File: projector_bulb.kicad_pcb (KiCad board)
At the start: 2 copper layers, 85.4 x 85.3 mm, 28 parts, among them J1 AC_1, J10 mount_2, J3 AC_2, J9 mount_1, U1 AL8860, U2 L7815

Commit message: Revision 2, still needs documentation and things
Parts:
- removed JP2: Jumper_2_Bridged, Jumper:SolderJumper-2_P1.3mm_Bridged_RoundedPad1.0x1.5mm
- added JP1: Jumper_2_Bridged, Jumper:SolderJumper-2_P1.3mm_Bridged_RoundedPad1.0x1.5mm, F.Cu at (140.7, 15.4)
- C1, C2: footprint Capacitor_THT:CP_Radial_D16.0mm_P7.50mm -> Capacitor_THT:CP_Radial_D12.5mm_P5.00mm
- C5: value 4.7u -> 22u
- R2: value 51k -> 7.5k
- U1: value AL8860 -> PAM2863; footprint Package_TO_SOT_SMD:TSOT-23-5_HandSoldering -> Package_SO:HTSOP-8-1EP_3.9x4.9mm_P1.27mm_EP2.4x3.2mm
- U2: value L7815 -> AP7381-33Y; footprint Package_TO_SOT_SMD:TO-263-2 -> Package_TO_SOT_SMD:SOT-89-3
- moved C5 11.0 mm to (117.3, 57.7), turned to 90 degrees
- moved D2 9.27 mm to (111.8, 45.7), turned to 90 degrees
- moved U1 6.40 mm to (112.8, 57.6), turned to 270 degrees
- moved R1 4.81 mm to (118.4, 50.3), turned to 180 degrees
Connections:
- C5 pad 1: Net-(C5-Pad1) -> GND_UPRIGHT
- C5 pad 2: Net-(C5-Pad2) -> VIN_UPRIGHT
- D2 pad 1: Net-(C5-Pad1) -> VIN_UPRIGHT
- J10 pad 1: Net-(J10-Pad1) -> (no net)
- J9 pad 1: Net-(J9-Pad1) -> (no net)
- R1 pad 1: Net-(C5-Pad1) -> VIN_UPRIGHT
- R2 pad 1: Net-(C5-Pad1) -> Net-(R2-Pad1)
- REF** pad 1: Net-(C5-Pad2) -> GND_UPRIGHT (x2)
- REF** pad 1: Net-(J5-Pad1) -> VIN_UPRIGHT (x2)
- RV1 pad 1: Net-(C5-Pad2) -> Net-(R2-Pad1)
- RV1 pad 3: Net-(R2-Pad2) -> GND_UPRIGHT
- U1 pad 1: Net-(D2-Pad2) -> VIN_UPRIGHT
- U1 pad 2: Net-(C5-Pad2) -> Net-(J8-Pad1)
- U1 pad 3: Net-(JP2-Pad1) -> GND_UPRIGHT
- U1 pad 4: Net-(J8-Pad1) -> DIMMING
- U1 pad 5: Net-(C5-Pad1) -> Net-(D2-Pad2)
- U2 pad 1: Net-(J5-Pad1) -> Net-(R2-Pad2)
- U2 pad 2: Net-(C5-Pad2) -> GND_UPRIGHT
- U2 pad 3: Net-(C5-Pad1) -> VIN_UPRIGHT
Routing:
- net GND_UPRIGHT: track 0.00 -> 125.3 mm, vias 0 -> 2
- net Net-(C5-Pad2): track 111.7 -> 0.00 mm, vias 11 -> 0
- net Net-(C5-Pad1): track 104.8 -> 0.00 mm, vias 2 -> 0
- net VIN_UPRIGHT: track 0.00 -> 77.7 mm, vias 0 -> 1
- net DIMMING: track 0.00 -> 67.0 mm, vias 0 -> 2
- net Net-(R2-Pad2): track 6.84 -> 67.8 mm, vias 0 -> 2
- net Net-(JP1-Pad1): track 53.4 -> 5.39 mm
- net Net-(J5-Pad1): track 22.0 -> 0.00 mm, vias 1 -> 0
- net Net-(JP2-Pad1): track 17.9 -> 0.00 mm, vias 1 -> 0
- net Net-(J8-Pad1): track 53.1 -> 44.0 mm, vias 2 -> 8
- net Net-(R2-Pad1): track 0.00 -> 9.05 mm
- net Net-(J7-Pad1): track 29.1 -> 22.5 mm, vias 1 -> 7
- net Net-(D2-Pad2): track 49.4 -> 50.6 mm
- removed copper zone on B.Cu, net Net-(C5-Pad2)
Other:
- board text added: "LED DCA Lamp Revision 2 April 2021"
- board text added: "LED front on this side"
- board text added: "ettingersam@gmail.com"

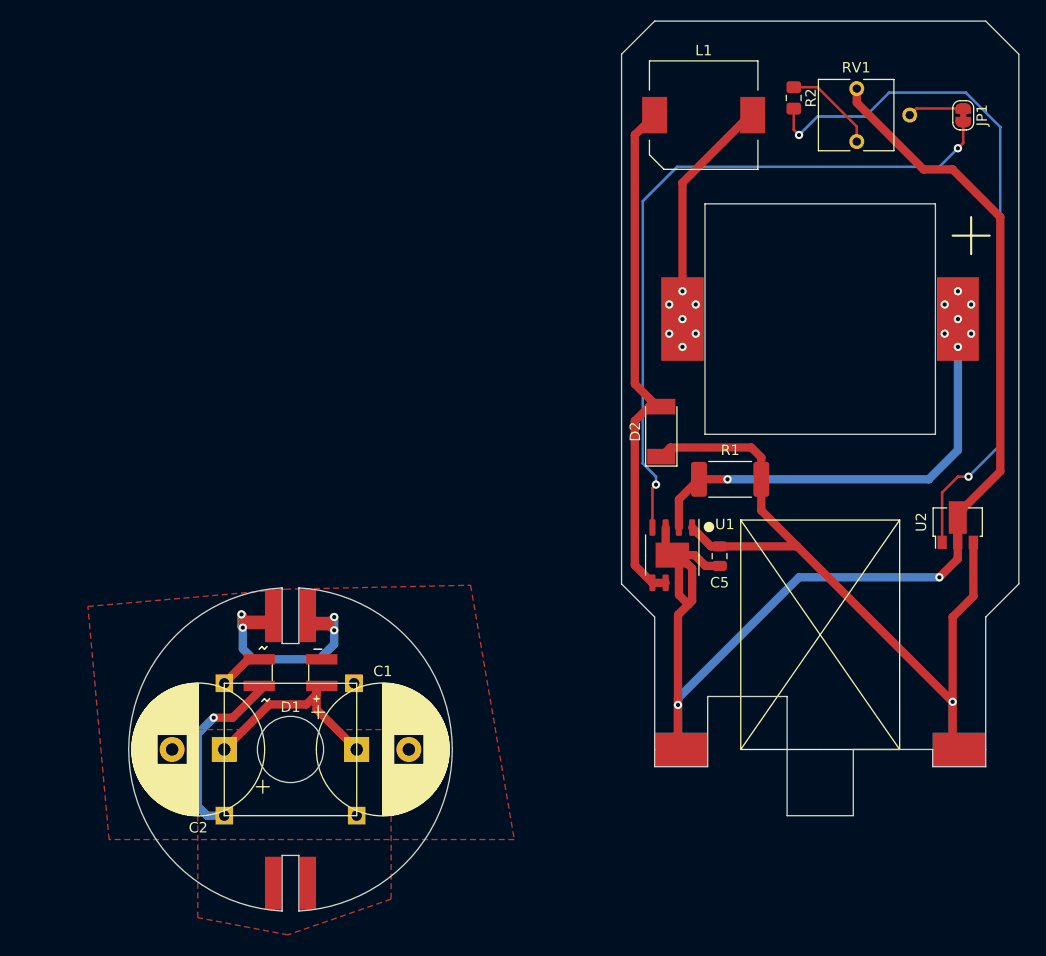
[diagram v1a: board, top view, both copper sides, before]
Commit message: Much progress on Aluminum PCB
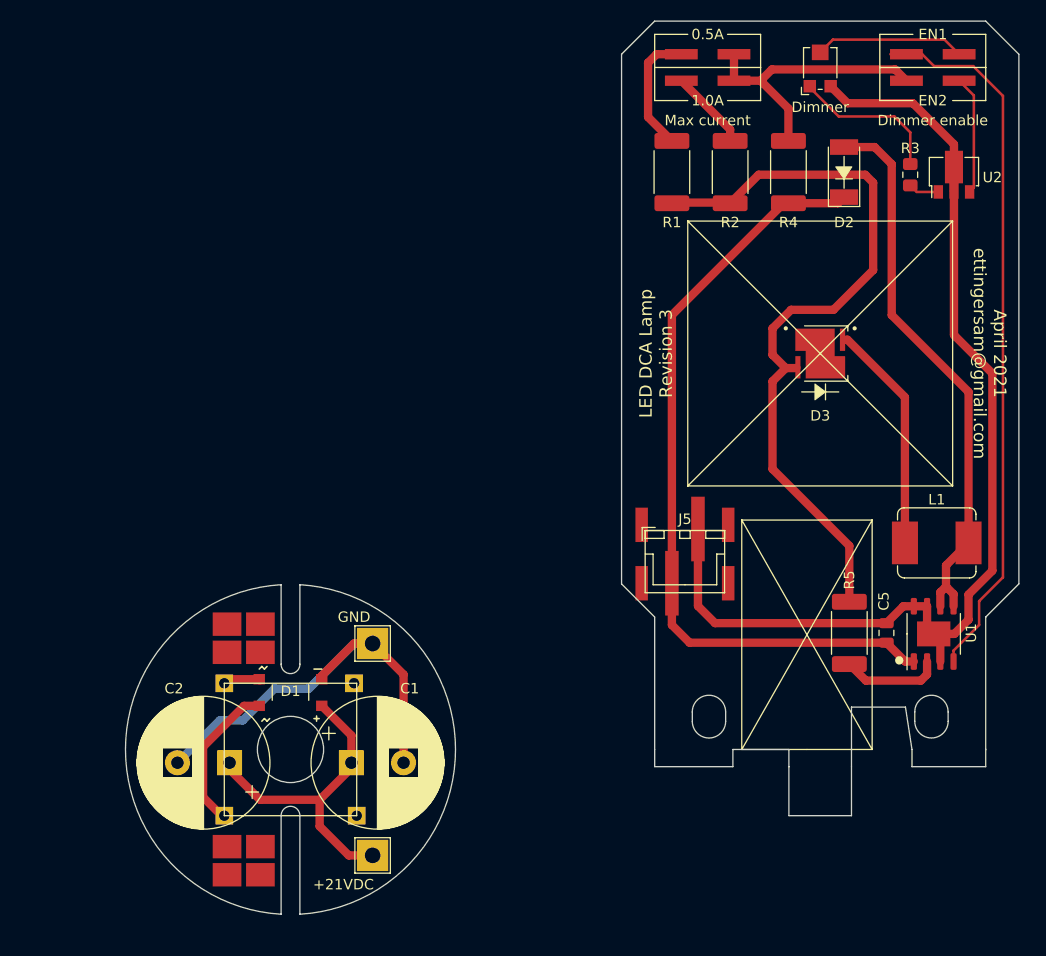
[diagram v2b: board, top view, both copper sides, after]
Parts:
- removed JP1: Jumper_2_Bridged, Jumper:SolderJumper-2_P1.3mm_Bridged_RoundedPad1.0x1.5mm
- removed REF** (x12): angle_joint, projector_bulb:angle_joint
- added +21VDC: to_upright_+, TestPoint:TestPoint_THTPad_3.0x3.0mm_Drill1.5mm, F.Cu at (84.1, 86.4)
- added D3: LED_Small_ALT, LED_SMD:LED_Cree-XHP50_12V, F.Cu at (127.0, 38.2)
- added GND: to_upright_-, TestPoint:TestPoint_THTPad_3.0x3.0mm_Drill1.5mm, F.Cu at (84.1, 66.0)
- added J11: mount_2, projector_bulb:wuerth_7466303R, F.Cu at (71.7, 65.5)
- added J12: mount_1, projector_bulb:wuerth_7466303R, F.Cu at (71.7, 86.9)
- added J5: to_base, projector_bulb:JST_XA_1x02_P2.50mm_SMD, F.Cu at (112.8, 57.7)
- added J7: Conn_02x02_Odd_Even, Connector_PinHeader_2.54mm:PinHeader_2x02_P2.54mm_Vertical_SMD, F.Cu at (116.2, 10.8)
- added J8: Conn_02x02_Odd_Even, Connector_PinHeader_2.54mm:PinHeader_2x02_P2.54mm_Vertical_SMD, F.Cu at (137.8, 10.8)
- added R2: 0.200, Resistor_SMD:R_2512_6332Metric_Pad1.52x3.35mm_HandSolder, F.Cu at (118.4, 20.8)
- added R4: 0Ω, Resistor_SMD:R_2512_6332Metric_Pad1.52x3.35mm_HandSolder, F.Cu at (124.0, 20.8)
- added R5: 0Ω, Resistor_SMD:R_2512_6332Metric_Pad1.52x3.35mm_HandSolder, F.Cu at (129.8, 65.0)
- C1, C2: value 2200u -> 1000μ
- L1: footprint projector_bulb:L_Wuerth_WE-PD-100100 -> projector_bulb:L_KEMET_MPLCV_0654_7.9x6.5mm
- RV1: footprint Potentiometer_THT:Potentiometer_Vishay_T73YP_Vertical -> Potentiometer_SMD:Potentiometer_Bourns_TC33X_Vertical
- moved L1 46.7 mm to (138.2, 56.4)
- moved U2 33.6 mm to (139.8, 21.1)
- moved D2 30.4 mm to (129.3, 20.8)
- moved R1 30.0 mm to (112.8, 20.8), turned to 270 degrees
- moved U1 26.2 mm to (137.9, 65.1), turned to 90 degrees
- moved C5 17.6 mm to (133.3, 65.0), turned to 270 degrees
- moved R3 13.4 mm to (135.6, 21.1)
- moved RV1 7.92 mm to (127.0, 10.8), turned to 90 degrees
- moved D1 1.91 mm to (76.2, 70.7)
- moved C2 1.37 mm to (70.4, 77.5)
- moved C1 1.37 mm to (82.0, 77.5)
- renumbered R2 to R3
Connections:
- net GND renamed GND_BASE
- net Net-(C1-Pad1) renamed VIN_BASE
- L1 pad 1: Net-(D2-Pad2) -> Net-(D3-Pad1)
- L1 pad 2: Net-(J7-Pad1) -> Net-(D2-Pad2)
- R1 pad 1: VIN_UPRIGHT -> Net-(J7-Pad1)
- R1 pad 2: Net-(J8-Pad1) -> CURRENT_SELECT
- U1 pad 2: Net-(J8-Pad1) -> Net-(R5-Pad2)
- U2 pad 3: VIN_UPRIGHT -> Net-(J8-Pad4)
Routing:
- net CURRENT_SELECT: track 0.00 -> 72.6 mm
- net Net-(R3-Pad2): track 67.8 -> 2.95 mm, vias 2 -> 0
- net Net-(J8-Pad1): track 44.0 -> 0.00 mm, vias 8 -> 0
- net VIN_NET_TIE: track 0.00 -> 26.9 mm
- net GND_UPRIGHT: track 125.3 -> 102.6 mm, vias 2 -> 0
- net Net-(D3-Pad1): track 0.00 -> 22.1 mm
- net GND_BASE: track 30.3 -> 42.6 mm, vias 4 -> 0
- net Net-(J8-Pad4): track 0.00 -> 11.4 mm
- net Net-(J7-Pad1): track 22.5 -> 12.0 mm, vias 7 -> 0
- net VIN_BASE: track 19.5 -> 29.3 mm
- net Net-(R5-Pad2): track 0.00 -> 9.59 mm
- net Net-(J8-Pad2): track 5.39 -> 14.4 mm
- net Net-(J7-Pad3): track 0.00 -> 7.72 mm
- net Net-(R3-Pad1): track 9.05 -> 14.6 mm
- net Net-(D2-Pad2): track 50.6 -> 54.7 mm
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- removed copper zone on F.Cu, net GND_BASE
- removed copper zone on F.Cu, net VIN_BASE
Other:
- board size 85.4 x 85.3 mm -> 85.7 x 85.7 mm
- board text added: "0.5A"
- board text added: "1.0A"
- board text added: "April 2021 ettingersam@gmail.com"
- board text added: "Dimmer"
- board text added: "Dimmer enable"
- board text added: "EN1"
- board text added: "EN2"
- board text added: "LED DCA Lamp Revision 3"
- board text added: "Max current"
- board text removed: "LED DCA Lamp Revision 2 April 2021"
- board text removed: "LED front on this side"
- board text removed: "ettingersam@gmail.com"

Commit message: More changes, about to add some safety circuitry
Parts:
- added R6: 1M, Resistor_SMD:R_0805_2012Metric_Pad1.15x1.40mm_HandSolder, F.Cu at (85.9, 69.8)
- added REF**: Fuse_1206_3216Metric, Fuse:Fuse_1206_3216Metric, F.Cu at (69.2, 65.0)
- added REF**: LENS_LEDIL_CA16370_HB-SQ-W, projector_bulb:LENS_LEDIL_CA16370_HB-SQ-W, F.Cu at (127.0, 38.2)
- J11, J12: footprint projector_bulb:wuerth_7466303R -> projector_bulb:wuerth_7466310R
- J5: footprint projector_bulb:JST_XA_1x02_P2.50mm_SMD -> Connector_Molex:Molex_CLIK-Mate_505405-0270_1x02-1MP_P1.50mm_Vertical
- moved J12 1.97 mm to (73.4, 87.9), turned to 90 degrees
- moved J11 1.97 mm to (73.4, 64.5), turned to 90 degrees
- moved J5 1.08 mm to (113.5, 56.9)
- renumbered +21VDC to J2, GND to J4
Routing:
- net VIN_BASE: track 29.3 -> 35.5 mm
- net GND_UPRIGHT: track 102.6 -> 98.5 mm
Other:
- outline, holes or cut-outs redrawn

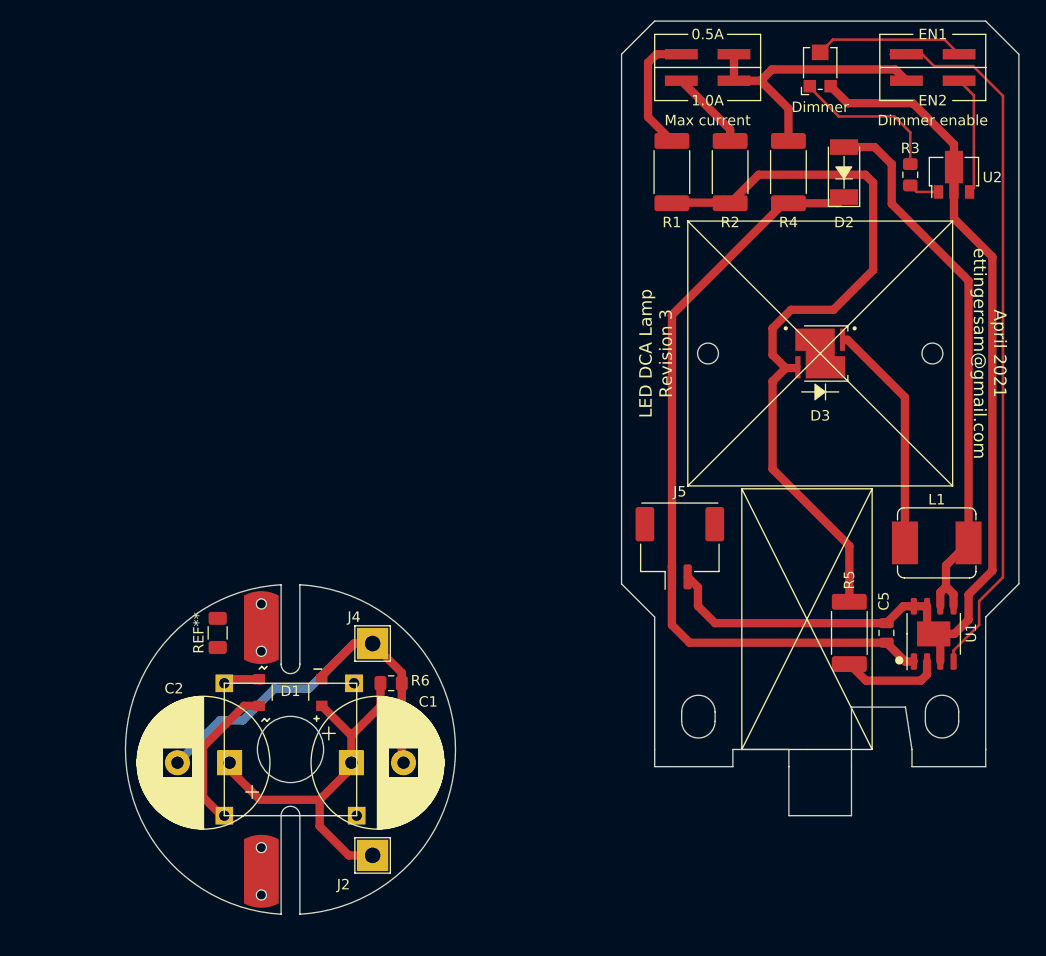
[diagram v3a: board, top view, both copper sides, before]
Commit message: Cleaned up schematic, working on documentation next
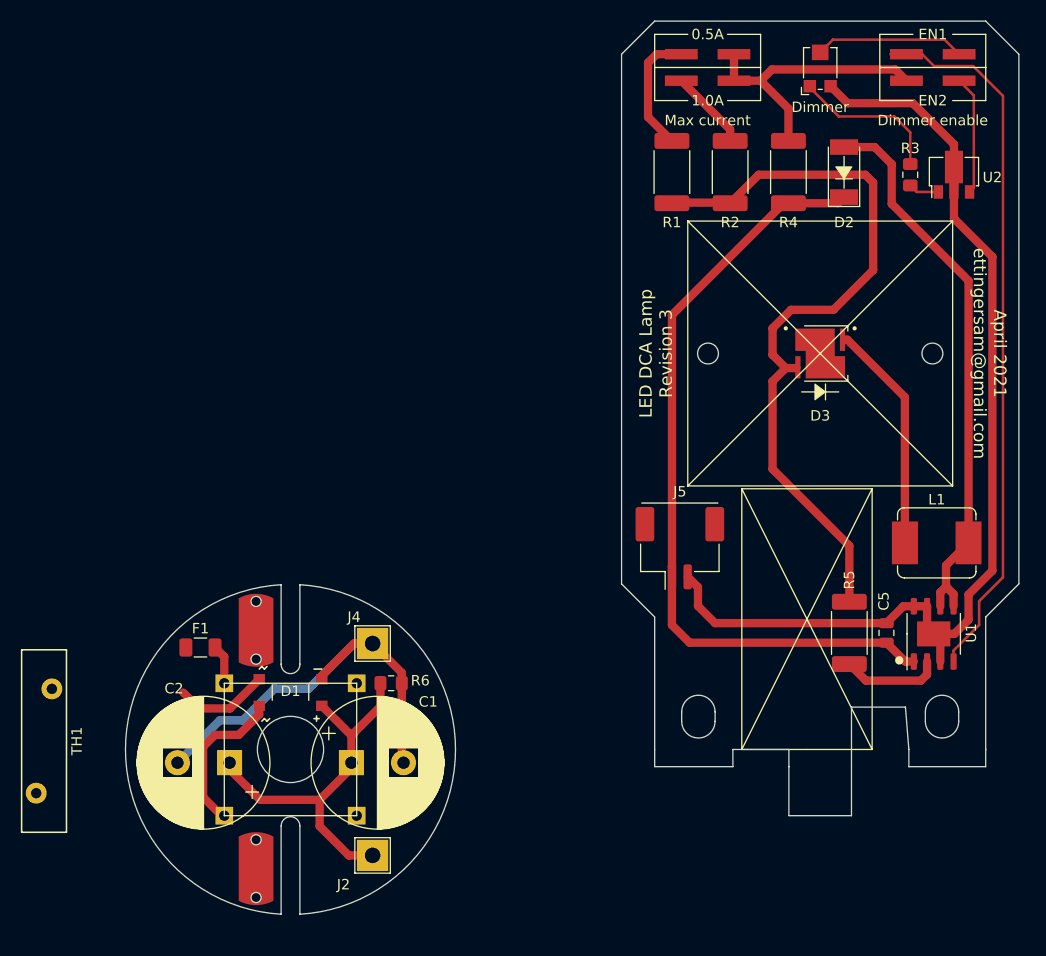
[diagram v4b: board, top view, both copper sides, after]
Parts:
- removed J1: AC_1, Connector_PinSocket_2.54mm:PinSocket_1x01_P2.54mm_Vertical
- removed J10: mount_2, Connector_PinSocket_2.54mm:PinSocket_1x01_P2.54mm_Vertical
- removed J11: mount_2, projector_bulb:wuerth_7466310R
- removed J12: mount_1, projector_bulb:wuerth_7466310R
- removed J3: AC_2, Connector_PinSocket_2.54mm:PinSocket_1x01_P2.54mm_Vertical
- removed J9: mount_1, Connector_PinSocket_2.54mm:PinSocket_1x01_P2.54mm_Vertical
- removed the REF** at (69.2, 65.0)
- added F1: Fuse, Fuse:Fuse_1206_3216Metric, F.Cu at (67.6, 66.4)
- added H1: MountingHole, projector_bulb:wuerth_7466310R, F.Cu at (72.9, 64.8)
- added H2: MountingHole, projector_bulb:wuerth_7466310R, F.Cu at (72.9, 87.6)
- added LA1: Lamp, projector_bulb:GX17q, B.Cu at (76.2, 76.2)
- added TH1: Thermistor_NTC, Varistor:RV_Disc_D21.5mm_W4.3mm_P10mm, F.Cu at (51.8, 80.4)
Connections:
- net CURRENT_SELECT renamed Net-(D3-Pad2)
- net VIN_NET_TIE renamed Net-(J7-Pad2)
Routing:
- net Net-(D1-Pad3): track 3.61 -> 9.25 mm
- net Net-(F1-Pad2): track 0.00 -> 3.80 mm
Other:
- outline, holes or cut-outs redrawn

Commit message: Add test points, replaced some expensive components with cheaper alternatives
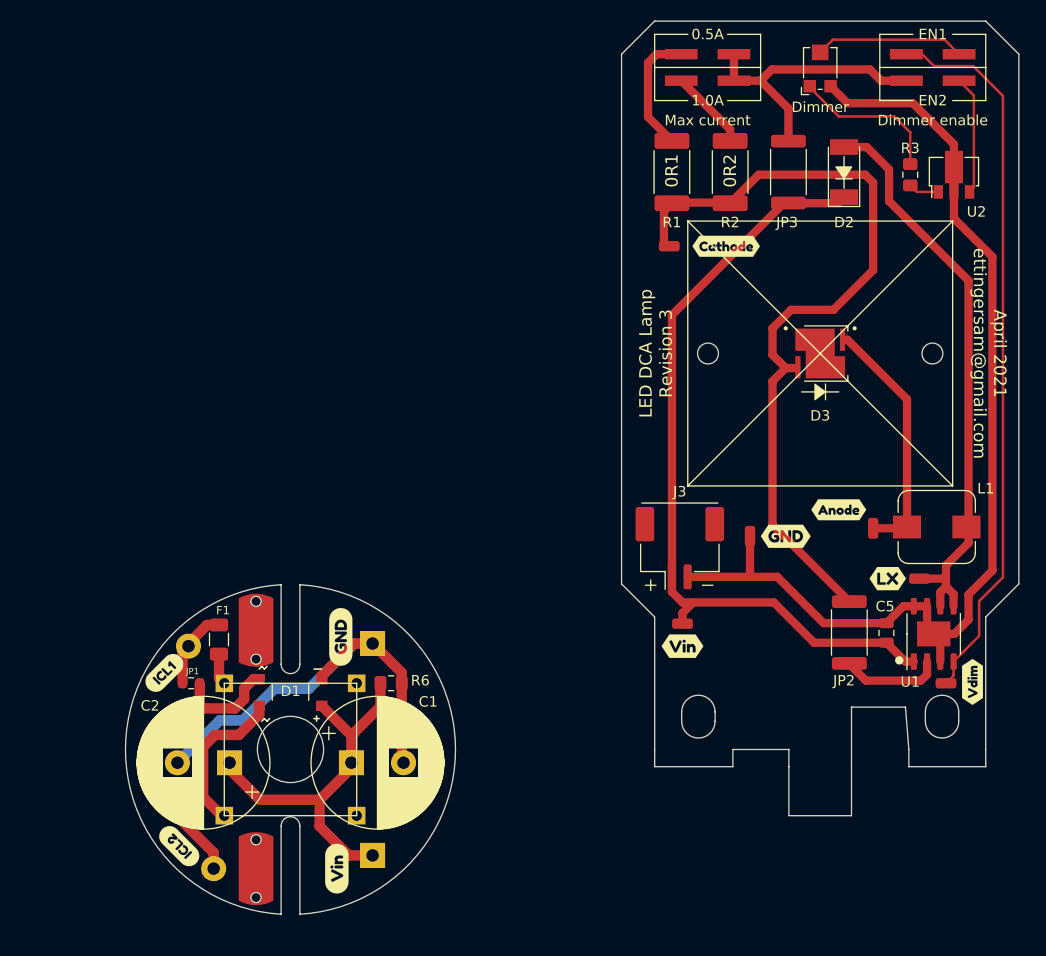
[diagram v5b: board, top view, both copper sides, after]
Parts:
- removed R4, R5: 0Ω, Resistor_SMD:R_2512_6332Metric_Pad1.52x3.35mm_HandSolder
- removed REF**: LENS_LEDIL_CA16370_HB-SQ-W, projector_bulb:LENS_LEDIL_CA16370_HB-SQ-W
- added HS1: Heatsink, projector_bulb:Heatsink_35x35x18mm, B.Cu at (127.0, 33.0)
- added JP1: ICL Bypass, Resistor_SMD:R_0603_1608Metric, F.Cu at (66.7, 69.8)
- added JP2: Jumper_NC_Small, Resistor_SMD:R_2512_6332Metric, F.Cu at (129.8, 65.0)
- added JP3: Jumper_NC_Small, Resistor_SMD:R_2512_6332Metric, F.Cu at (124.0, 20.8)
- added LENS1: Lens, projector_bulb:LENS_LEDIL_CA16370_HB-SQ-W, F.Cu at (127.0, 38.2)
- added TP1: TestPoint, projector_bulb:Test_Point_0603, F.Cu at (113.8, 64.1)
- added TP2: TestPoint, projector_bulb:Test_Point_0603, F.Cu at (120.3, 55.8)
- added TP3: TestPoint, projector_bulb:Test_Point_0603, F.Cu at (136.5, 59.8)
- added TP4: TestPoint, projector_bulb:Test_Point_0603, F.Cu at (139.1, 69.8)
- added TP5: TestPoint, projector_bulb:Test_Point_0603, F.Cu at (112.5, 27.9)
- added TP6: TestPoint, projector_bulb:Test_Point_0603, F.Cu at (132.1, 55.0)
- added svg2mod: G***, label, F.Cu at (128.8, 53.2)
- added svg2mod: G***, label, F.Cu at (63.8, 70.0)
- added svg2mod: G***, label, F.Cu at (118.0, 27.9)
- added svg2mod: G***, label, F.Cu at (141.6, 69.7)
- added svg2mod: G***, label, F.Cu at (133.5, 59.8)
- added svg2mod: G***, label, F.Cu at (113.8, 66.3)
- added svg2mod: G***, label, F.Cu at (123.7, 55.8)
- added svg2mod: G***, label, F.Cu at (81.0, 65.4)
- added svg2mod: G***, label, F.Cu at (80.6, 87.6)
- added svg2mod: G***, label, F.Cu at (65.5, 85.5)
- L1: footprint projector_bulb:L_KEMET_MPLCV_0654_7.9x6.5mm -> projector_bulb:panasonic_PCC-M0748M
- moved TH1 13.2 mm to (64.9, 82.0)
- moved F1 1.93 mm to (69.3, 65.7), turned to 270 degrees
- moved L1 1.52 mm to (138.2, 54.9)
- renumbered J2 to J1, J4 to J2, J5 to J3, J7 to J4, J8 to J5
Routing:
- net Net-(D1-Pad3): track 9.25 -> 31.0 mm
- net Net-(F1-Pad1): track 0.00 -> 7.27 mm
- net Net-(D3-Pad2): track 72.6 -> 76.7 mm
- net GND_UPRIGHT: track 98.5 -> 101.3 mm
- net DIMMING: track 68.7 -> 71.0 mm
- net Net-(D2-Pad2): track 54.7 -> 56.9 mm
- net Net-(D3-Pad1): track 22.1 -> 24.0 mm
- net Net-(F1-Pad2): track 3.80 -> 2.50 mm
- net VIN_UPRIGHT: track 76.4 -> 77.0 mm
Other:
- net class Base Track added: clearance 0.25, trace_width 1, via_dia 0.8, via_drill 0.4
- board text added: "0R1"
- board text added: "0R2"

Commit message: Making edits
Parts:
- D2: footprint Diode_SMD:D_MELF -> Diode_SMD:D_SOD-123F
- renumbered C5 to C3, R6 to R4
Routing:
- net Net-(D3-Pad2): track 76.7 -> 70.8 mm
- net Net-(D2-Pad2): track 56.9 -> 55.4 mm
- net VIN_UPRIGHT: track 77.0 -> 78.0 mm
